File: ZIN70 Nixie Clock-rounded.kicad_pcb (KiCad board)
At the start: 2 copper layers, 270 x 90 mm, 43 parts, among them U1 HV5122, U2 HV5122, U3 CD40109BPW

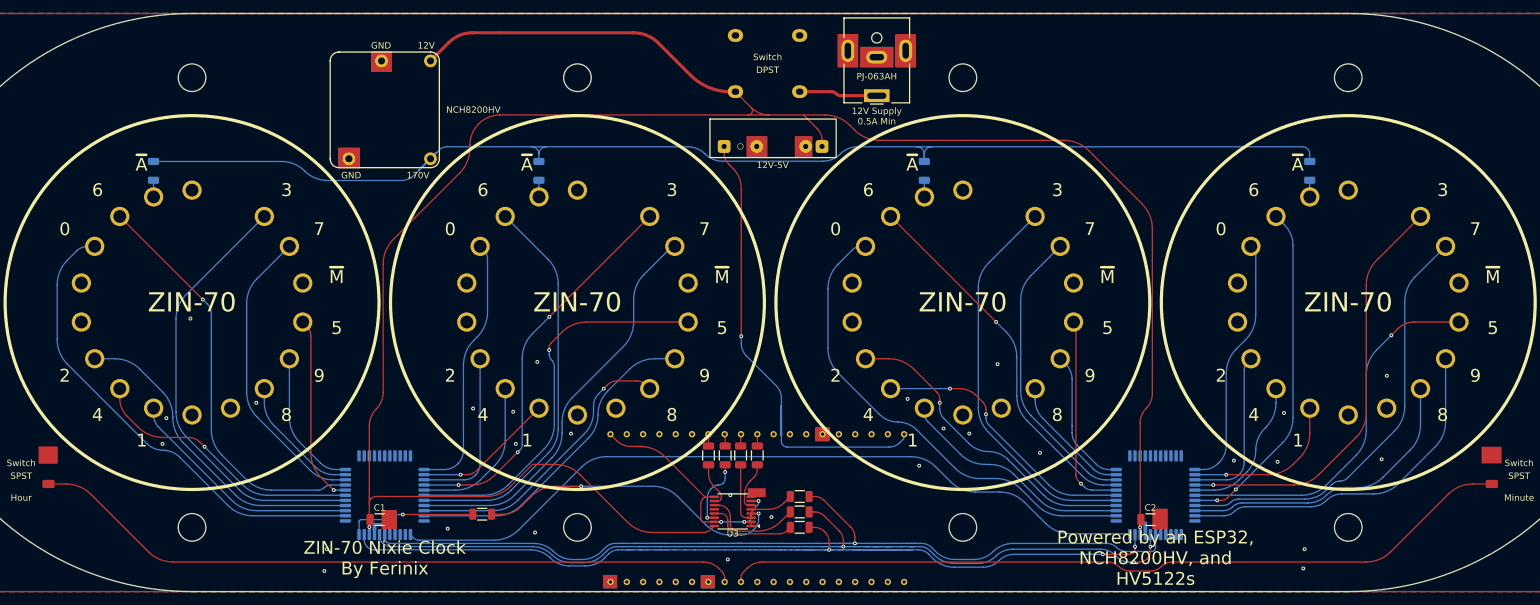
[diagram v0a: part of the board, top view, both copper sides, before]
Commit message: Update the clock with 5mm indicators
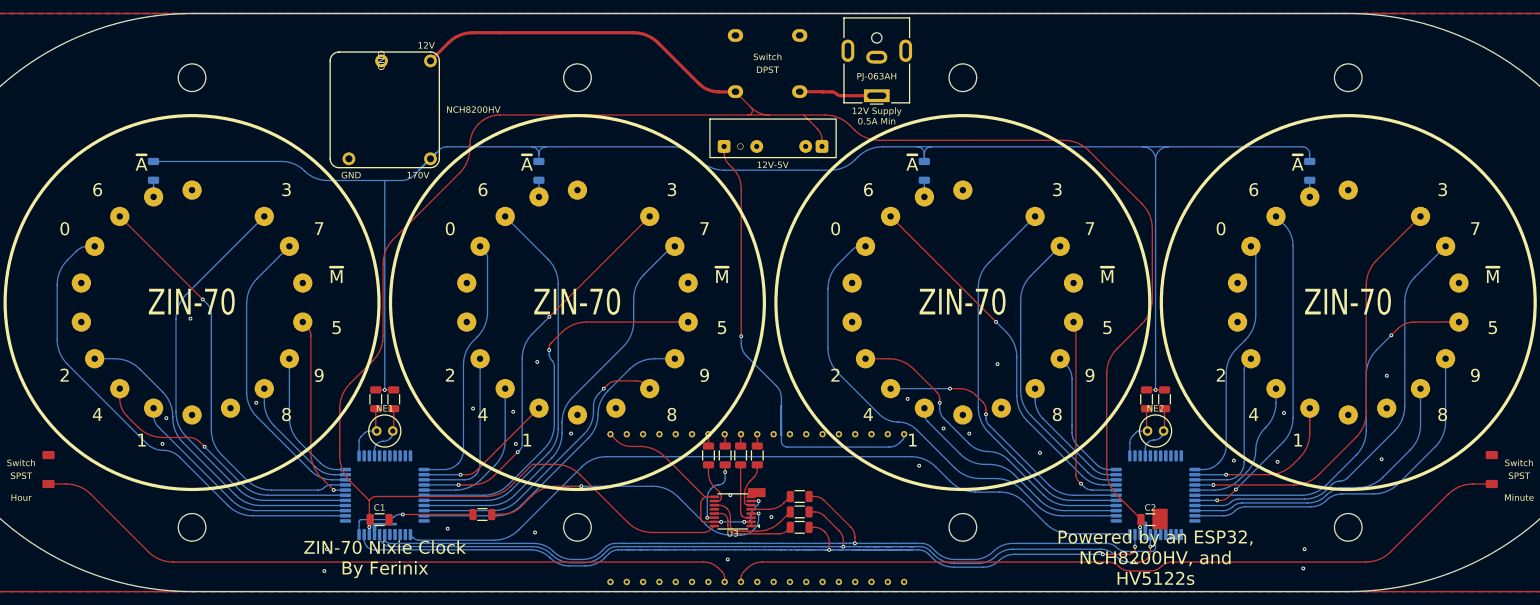
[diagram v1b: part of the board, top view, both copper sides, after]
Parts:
- added NE1: NE-2, NixFootprints:NE-2_5mm, F.Cu at (130.0, 120.0)
- added NE2: NE-2, NixFootprints:NE-2_5mm, F.Cu at (250.0, 120.0)
- added R10: 1K, Resistor_SMD:R_1206_3216Metric, F.Cu at (194.6, 132.6)
- added R11: 1K, Resistor_SMD:R_1206_3216Metric, F.Cu at (194.6, 130.2)
- added R12: 1K, Resistor_SMD:R_1206_3216Metric, F.Cu at (145.2, 133.0)
- added R9: 1K, Resistor_SMD:R_1206_3216Metric, F.Cu at (194.6, 135.0)
- R5, R6, R7, R8: value 1K -> 100K
- moved R6 65.0 mm to (131.4, 115.1), turned to 90 degrees
- moved R8 60.2 mm to (251.4, 115.1), turned to 90 degrees
- moved R7 56.8 mm to (248.6, 115.1), turned to 90 degrees
- moved R5 24.4 mm to (128.6, 115.1), turned to 90 degrees
- renumbered ZIN-70 to NIX1, ZIN-70 to NIX2, ZIN-70 to NIX3, ZIN-70 to NIX4, R9 to R13, R10 to R14, R11 to R15, R12 to R16
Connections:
- R5 pad 1: Net-(U1-DIN) -> Net-(U1-HV11)
- R5 pad 2: Net-(U3-E) -> +170V
- R6 pad 1: Net-(U1-~{OE}) -> Net-(U1-HV14)
- R6 pad 2: Net-(U3-F) -> +170V
- R7 pad 1: Net-(U1-CLK) -> Net-(U2-HV11)
- R7 pad 2: Net-(U3-G) -> +170V
- R8 pad 1: Net-(U1-STR) -> Net-(U2-HV14)
- R8 pad 2: Net-(U3-H) -> +170V
- U1 pad 1: unconnected-(U1-HV11-Pad1) -> Net-(U1-HV11)
- U1 pad 4: unconnected-(U1-HV14-Pad4) -> Net-(U1-HV14)
- U2 pad 1: unconnected-(U2-HV11-Pad1) -> Net-(U2-HV11)
- U2 pad 4: unconnected-(U2-HV14-Pad4) -> Net-(U2-HV14)
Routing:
- net +170V: track 196.4 -> 277.5 mm, vias 0 -> 2
- net Net-(U2-HV11): track 0.00 -> 9.37 mm
- net Net-(U1-HV11): track 0.00 -> 9.37 mm
- net Net-(U2-HV14): track 0.00 -> 9.27 mm
- net Net-(U1-HV14): track 0.00 -> 9.06 mm
- net +12V: track 370.4 -> 375.5 mm
